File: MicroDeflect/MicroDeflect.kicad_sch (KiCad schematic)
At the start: 5 parts, among them J1 Conn_01x04

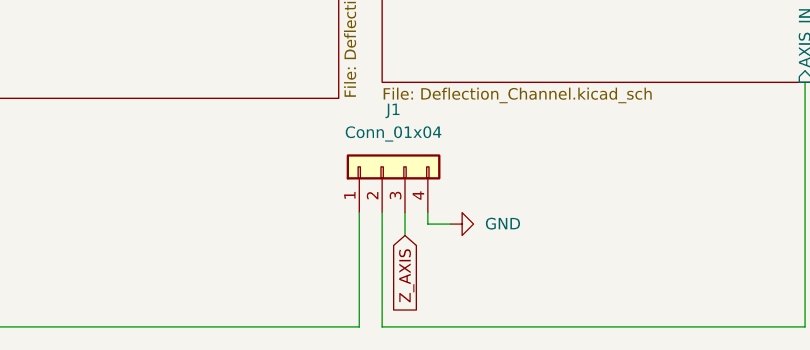
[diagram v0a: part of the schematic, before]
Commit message: Clean up KiCad rename artifacts; MicroDeflect is the project
Remove stray DeflectionBoard.* files and _restore_backup that KiCad
recreated when the old project was still open during the rename.
MicroDeflect.* (latest, 21:16) is the real work; project validated.

Co-Authored-By: Claude Opus 4.8 <noreply@anthropic.com>
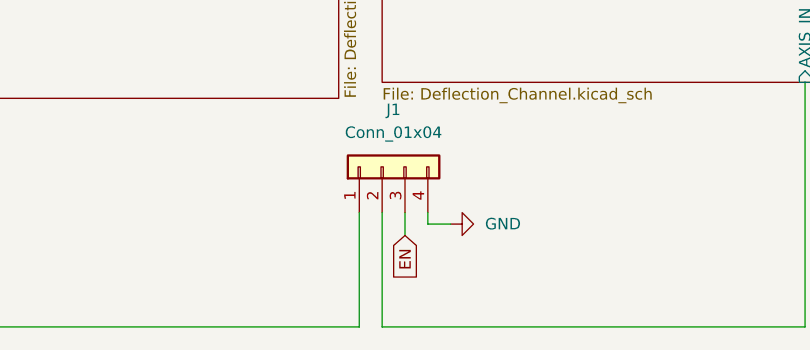
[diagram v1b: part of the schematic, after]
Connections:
- net Z_AXIS renamed EN
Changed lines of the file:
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@@
 		)
 	)
-	(global_label "Z_AXIS"
+	(global_label "EN"
 		(shape input)
 		(at 266.7 120.65 270)
@@
 		)
 		(property "Intersheetrefs" "${INTERSHEET_REFS}"
-			(at 266.7 129.9247 90)
+			(at 266.7 126.1147 90)
 			(hide yes)
 			(show_name no)

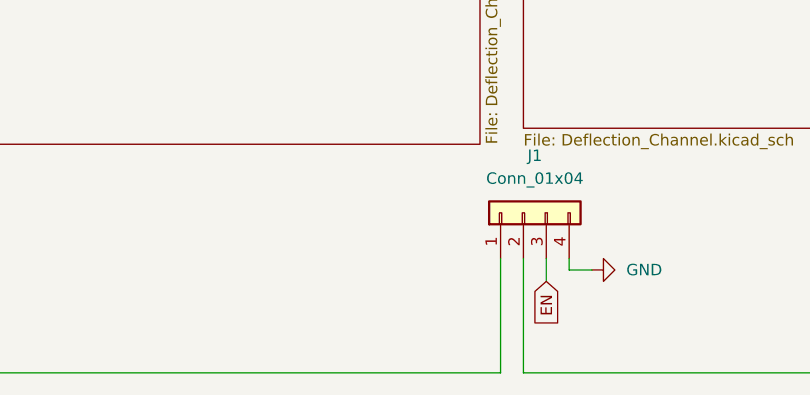
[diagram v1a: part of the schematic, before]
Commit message: MicroDeflect: add J2 (HV board interface), fix J1.3 = Z_AXIS
- J1.3 restored to Z_AXIS (was wrongly on EN); J1 = LogicBoard input (X/Y/Z/GND)
- J2 added = output to HV board: Z_AXIS (pass-through from J1.3), GND, EN
- EN net (R208 pull-up + AND gates) routed to J2.3 for HV spot-killer disable
- DRC: 0 unconnected (J2 placed + routed)

Co-Authored-By: Claude Opus 4.8 <noreply@anthropic.com>
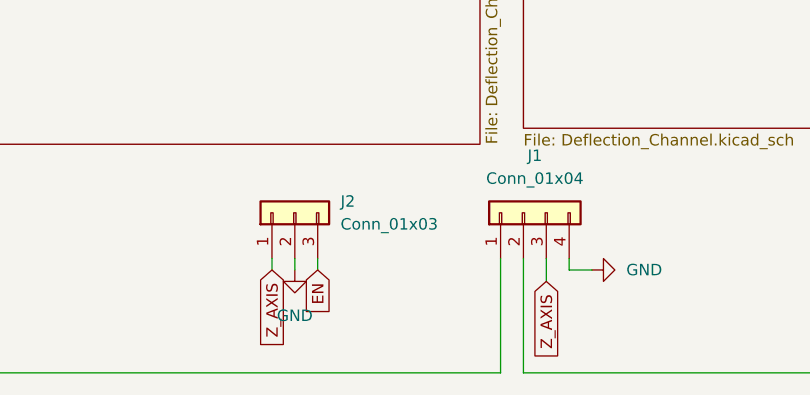
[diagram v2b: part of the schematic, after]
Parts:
- added J2: Conn_01x03, symbol Connector_Generic:Conn_01x03
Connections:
- net EN: now also J2.3 (Pin_3); no longer J1.3 (Pin_3)
- net GND: now also J2.2 (Pin_2)
- new net Z_AXIS: J1.3 (Pin_3), J2.1 (Pin_1)
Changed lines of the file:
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@@
+	(wire
+		(pts
+			(xy 241.3 118.11) (xy 241.3 119.38)
+		)
+		(stroke
+			(width 0)
+			(type default)
+		)
+	)
 	(wire
 		(pts
@@
 	(wire
 		(pts
+			(xy 238.76 118.11) (xy 238.76 119.38)
+		)
+		(stroke
+			(width 0)
+			(type default)
+		)
+	)
+	(wire
+		(pts
 			(xy 311.15 103.632) (xy 311.15 130.81)
 		)
@@
 		)
 	)
-	(global_label "EN"
+	(wire
+		(pts
+			(xy 236.22 118.11) (xy 236.22 119.38)
+		)
+		(stroke
+			(width 0)
+			(type default)
+		)
+	)
+	(global_label "Z_AXIS"
 		(shape input)
 		(at 266.7 120.65 270)
@@
 		)
 		(property "Intersheetrefs" "${INTERSHEET_REFS}"
-			(at 266.7 126.1147 90)
+			(at 266.7 129.9247 90)
+			(hide yes)
+			(show_name no)
+			(do_not_autoplace no)
+			(effects
+				(font
+					(size 1.27 1.27)
+				)
+				(justify right)
+			)
+		)
+	)
+	(global_label "Z_AXIS"
+		(shape input)
+		(at 236.22 119.38 270)
+		(fields_autoplaced yes)
+		(effects
+			(font
+				(size 1.27 1.27)
+			)
+			(justify right)
+		)
+		(property "Intersheetrefs" "${INTERSHEET_REFS}"
+			(at 236.22 128.6547 90)
+			(hide yes)
+			(show_name no)
+			(do_not_autoplace no)
+			(effects
+				(font
+					(size 1.27 1.27)
+				)
+				(justify right)
+			)
+		)
+	)
+	(global_label "EN"
+		(shape input)
+		(at 241.3 119.38 270)
+		(fields_autoplaced yes)
+		(effects
+			(font
+				(size 1.27 1.27)
+			)
+			(justify right)
+		)
+		(property "Intersheetrefs" "${INTERSHEET_REFS}"
+			(at 241.3 124.8447 90)
 			(hide yes)
 			(show_name no)
@@
 	)
 	(symbol
+		(lib_id "Connector_Generic:Conn_01x03")
+		(at 238.76 113.03 90)
+		(unit 1)
+		(body_style 1)
+		(exclude_from_sim no)
+		(in_bom yes)
+		(on_board yes)
+		(in_pos_files yes)
+		(dnp no)
+		(fields_autoplaced yes)
+		(property "Reference" "J2"
+			(at 243.84 111.7599 90)
+			(show_name no)
+			(do_not_autoplace no)
+			(effects
+				(font
+					(size 1.27 1.27)
+				)
+				(justify right)
+			)
+		)
+		(property "Value" "Conn_01x03"
+			(at 243.84 114.2999 90)
+			(show_name no)
+			(do_not_autoplace no)
+			(effects
+				(font
+					(size 1.27 1.27)
+				)
+				(justify right)
+			)
+		)
+		(property "Footprint" ""
+			(at 238.76 113.03 0)
+			(hide yes)
+			(show_name no)
+			(do_not_autoplace no)
+			(effects
+				(font
+					(size 1.27 1.27)
+				)
+			)
+		)
+		(property "Datasheet" ""
+			(at 238.76 113.03 0)
+			(hide yes)
+			(show_name no)
+			(do_not_autoplace no)
+			(effects
+				(font
+					(size 1.27 1.27)
+				)
+			)
+		)
+		(property "Description" "Generic connector, single row, 01x03, script generated (kicad-library-utils/schlib/autogen/connector/)"
+			(at 238.76 113.03 0)
+			(hide yes)
+			(show_name no)
+			(do_not_autoplace no)
+			(effects
+				(font
+					(size 1.27 1.27)
+				)
+			)
+		)
+		(pin "3"
+		)
+		(pin "1"
+		)
+		(pin "2"
+		)
+		(instances
+			(project "MicroDeflect"
+				(path "/6f717d52-0a9b-43ca-aa24-dc6f278930de"
+					(reference "J2")
+					(unit 1)
+				)
+			)
+		)
+	)
+	(symbol
 		(lib_id "Mechanical:MountingHole")
 		(at 85.09 125.73 0)
@@
 					(unit 1)
 				)
+			)
+		)
+	)
+	(symbol
+		(lib_id "power:GND")
+		(at 238.76 119.38 0)
+		(unit 1)
+		(body_style 1)
+		(exclude_from_sim no)
+		(in_bom yes)
+		(on_board yes)
+		(in_pos_files yes)
+		(dnp no)
+		(fields_autoplaced yes)
+		(property "Reference" "#PWR0302"
+			(at 238.76 125.73 0)
+			(hide yes)
+			(show_name no)
+			(do_not_autoplace no)
+			(effects
+				(font
+					(size 1.27 1.27)
+				)
+			)
+		)
+		(property "Value" "GND"
+			(at 238.76 124.46 0)
+			(show_name no)
+			(do_not_autoplace no)
+			(effects
+				(font
+					(size 1.27 1.27)
+				)
+			)
+		)
+		(property "Footprint" ""
+			(at 238.76 119.38 0)
+			(hide yes)
+			(show_name no)
+			(do_not_autoplace no)
+			(effects
+				(font
+					(size 1.27 1.27)
+				)
+			)
+		)
+		(property "Datasheet" ""
+			(at 238.76 119.38 0)
+			(hide yes)
+			(show_name no)
+			(do_not_autoplace no)
+			(effects
+				(font
+					(size 1.27 1.27)
+				)
+			)
+		)
+		(property "Description" "Power symbol creates a global label with name \"GND\" , ground"
+			(at 238.76 119.38 0)
+			(hide yes)
+			(show_name no)
+			(do_not_autoplace no)
+			(effects
+				(font
+					(size 1.27 1.27)
+				)
+			)
+		)
+		(pin "1"
+		)
+		(instances
+			(project "MicroDeflect"
+				(path "/6f717d52-0a9b-43ca-aa24-dc6f278930de"
+					(reference "#PWR0302")
+					(unit 1)
+				)
